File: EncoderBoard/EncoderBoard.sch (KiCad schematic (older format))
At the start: 6 parts, among them P1 CONN_01X02, P2 CONN_01X02, U1 RPI-579N1

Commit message: generate gerbers
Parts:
- removed P1, P2: CONN_01X02, Pin_Headers:Pin_Header_Straight_1x02, symbol CONN_01X02
- added P1: CONN_01X03, Pin_Headers:Pin_Header_Angled_1x03, symbol CONN_01X03
- U1: Fieldname (none) -> Value
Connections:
- net +5V: now also P1.3 (P3)
- net GND: now also P1.2 (P2)
- net Signal: now also P1.1 (P1)
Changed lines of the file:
@@
 F 1 "RPI-579N1" H 4740 3390 50  0000 L CNN
 F 2 "EncoderBoard:RPI-579N1" H 4730 3390 50  0001 L CIN
-F 3 "" H 4930 3590 50  0000 L CNN
+F 3 "http://www.mouser.com/ds/2/348/rpi-579n1-208956.pdf" H 4930 3590 50  0001 L CNN
+F 4 "Value" H 4930 3590 60  0001 C CNN "Fieldname"
 	1    4930 3590
 	1    0    0    -1
@@
 Wire Wire Line
 	4630 3690 4630 3830
-Wire Wire Line
-	3750 3830 5230 3830
 Connection ~ 5230 3830
 $Comp
@@
 	1    0    0    -1
 $EndComp
-$Comp
-L CONN_01X02 P1
-U 1 1 585FE506
-P 3800 2800
-F 0 "P1" H 3800 2950 50  0000 C CNN
-F 1 "CONN_01X02" V 3900 2800 50  0000 C CNN
-F 2 "Pin_Headers:Pin_Header_Straight_1x02" H 3800 2800 50  0001 C CNN
-F 3 "" H 3800 2800 50  0000 C CNN
-	1    3800 2800
-	0    -1   -1   0
-$EndComp
-$Comp
-L CONN_01X02 P2
-U 1 1 585FE579
-P 6010 2810
-F 0 "P2" H 6010 2960 50  0000 C CNN
-F 1 "CONN_01X02" V 6110 2810 50  0000 C CNN
-F 2 "Pin_Headers:Pin_Header_Straight_1x02" H 6010 2810 50  0001 C CNN
-F 3 "" H 6010 2810 50  0000 C CNN
-	1    6010 2810
-	0    1    -1   0
-$EndComp
-Wire Wire Line
-	3750 3000 3750 3830
 Connection ~ 4630 3830
 Wire Wire Line
-	5230 3740 6060 3740
-Wire Wire Line
-	6060 3740 6060 3010
-Connection ~ 5230 3740
-Wire Wire Line
 	5230 3410 5960 3410
-Wire Wire Line
-	5960 3410 5960 3010
 Connection ~ 5230 3410
-Wire Wire Line
-	3850 3000 5230 3000
 Wire Wire Line
 	4630 3080 4630 3000
@@
 	5540 3250 5540 3410
 Connection ~ 5540 3410
+$Comp
+L CONN_01X03 P1
+U 1 1 58619F19
+P 3130 3290
+F 0 "P1" H 3130 3490 50  0000 C CNN
+F 1 "CONN_01X03" V 3230 3290 50  0000 C CNN
+F 2 "Pin_Headers:Pin_Header_Angled_1x03" H 3130 3290 50  0001 C CNN
+F 3 "" H 3130 3290 50  0000 C CNN
+	1    3130 3290
+	-1   0    0    1
+$EndComp
+Wire Wire Line
+	3330 3000 5230 3000
+Wire Wire Line
+	3330 3000 3330 3190
+Wire Wire Line
+	3330 3290 4480 3290
+Wire Wire Line
+	4480 3290 4480 3830
+Wire Wire Line
+	4480 3830 5230 3830
+Wire Wire Line
+	5960 3410 5960 4050
+Wire Wire Line
+	5960 4050 3940 4050
+Wire Wire Line
+	3940 4050 3940 3390
+Wire Wire Line
+	3940 3390 3330 3390
 $EndSCHEMATC

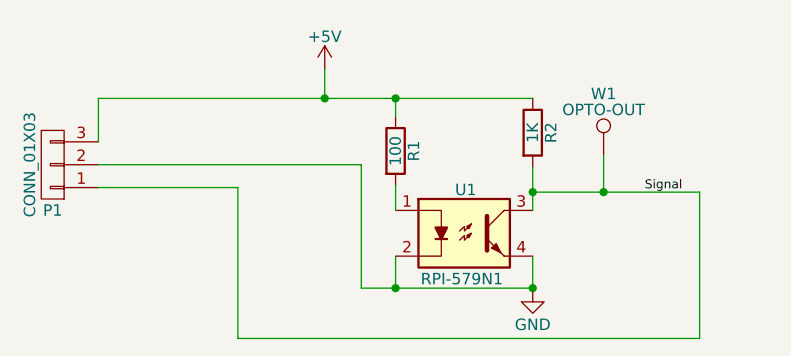
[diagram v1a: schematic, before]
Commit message: changed the pull up resistor to 3.3K
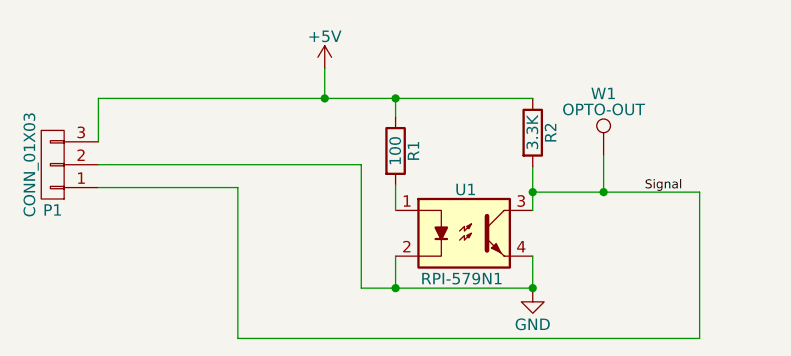
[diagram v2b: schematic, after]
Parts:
- R2: value 1K -> 3.3K
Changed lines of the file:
@@
 P 5230 3150
 F 0 "R2" V 5310 3150 50  0000 C CNN
-F 1 "1K" V 5230 3150 50  0000 C CNN
+F 1 "3.3K" V 5230 3150 50  0000 C CNN
 F 2 "Resistors_SMD:R_0805_HandSoldering" V 5160 3150 50  0001 C CNN
 F 3 "" H 5230 3150 50  0000 C CNN
